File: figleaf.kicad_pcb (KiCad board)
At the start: 2 copper layers, 150 x 105 mm, 31 parts, among them U1 Nice_Nano_V2_GRAZ

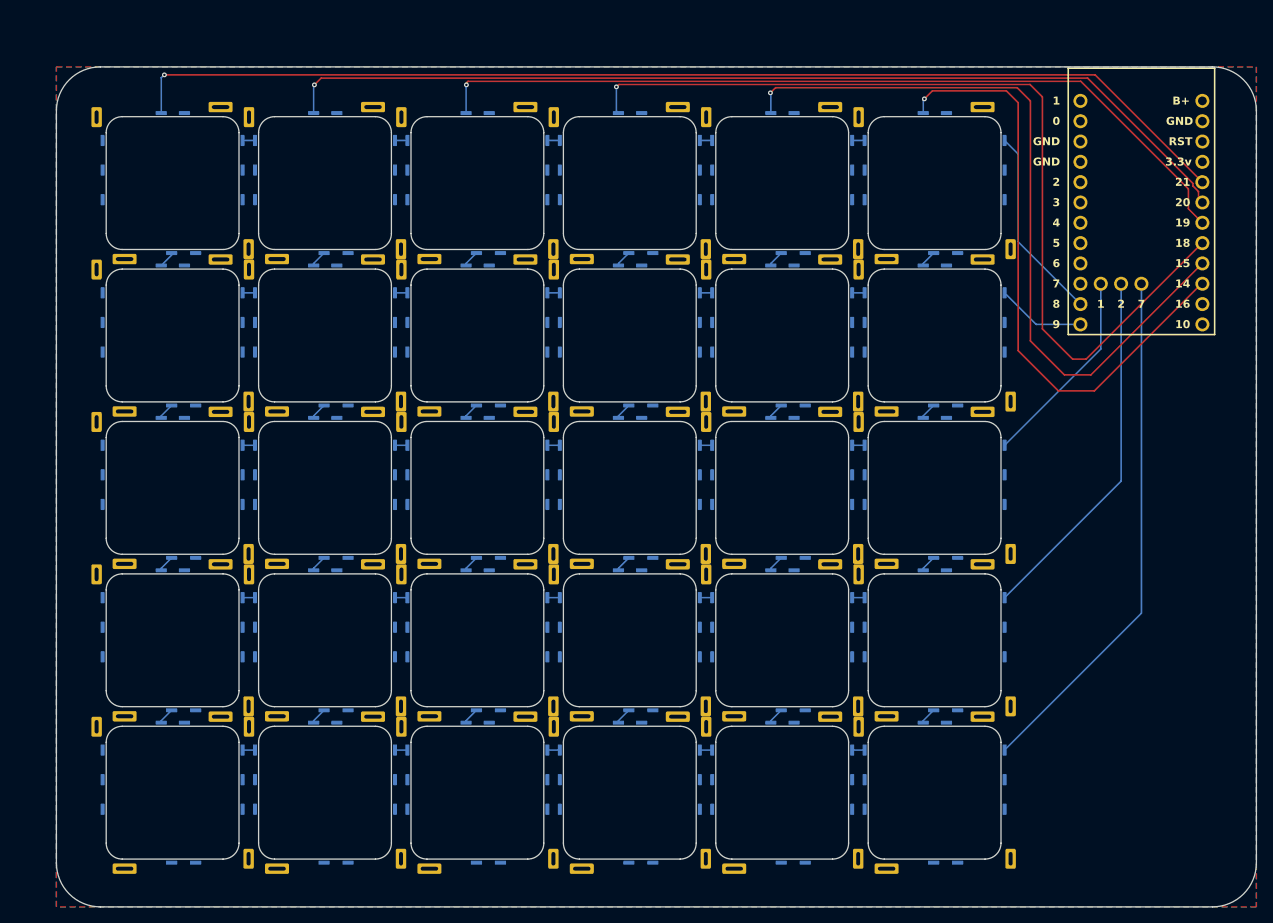
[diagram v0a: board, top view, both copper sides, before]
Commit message: PCB progress, switches to 19x19 pitch
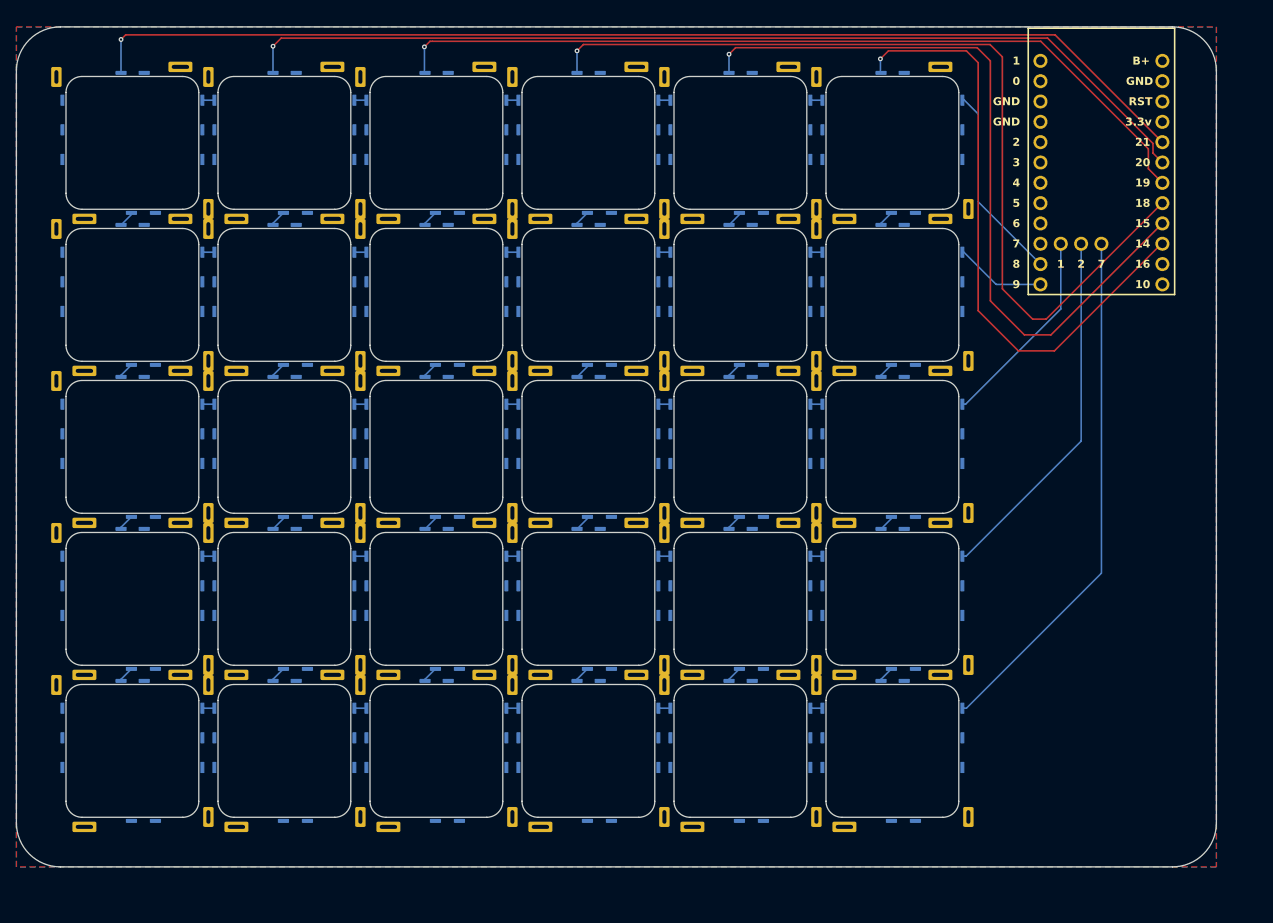
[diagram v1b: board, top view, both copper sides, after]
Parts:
- moved S30 7.42 mm to (129.5, 110.5)
- moved S24 7.39 mm to (129.5, 91.5)
- moved S29 7.39 mm to (110.5, 110.5)
- moved S18 7.35 mm to (129.5, 72.5)
- moved S23 7.35 mm to (110.5, 91.5)
- moved S28 7.35 mm to (91.5, 110.5)
- moved S12 7.32 mm to (129.5, 53.5)
- moved S17 7.32 mm to (110.5, 72.5)
- moved S27 7.32 mm to (72.5, 110.5)
- moved S22 7.32 mm to (91.5, 91.5)
- moved S6 7.29 mm to (129.5, 34.5)
- moved S11 7.28 mm to (110.5, 53.5)
- moved S26 7.28 mm to (53.5, 110.5)
- moved S16 7.28 mm to (91.5, 72.5)
- moved S21 7.28 mm to (72.5, 91.5)
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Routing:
- net col_3: track 114.0 -> 113.5 mm

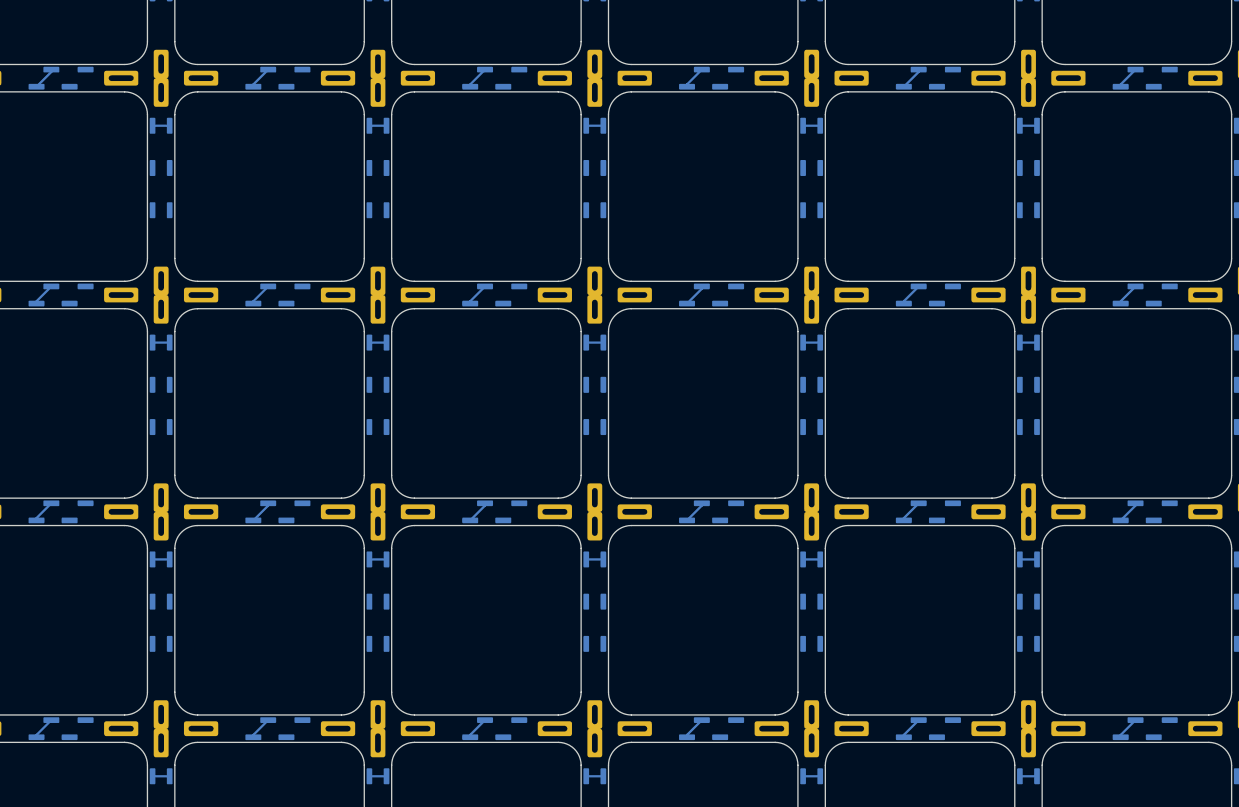
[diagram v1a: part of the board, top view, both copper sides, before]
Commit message: Add SW ground conn
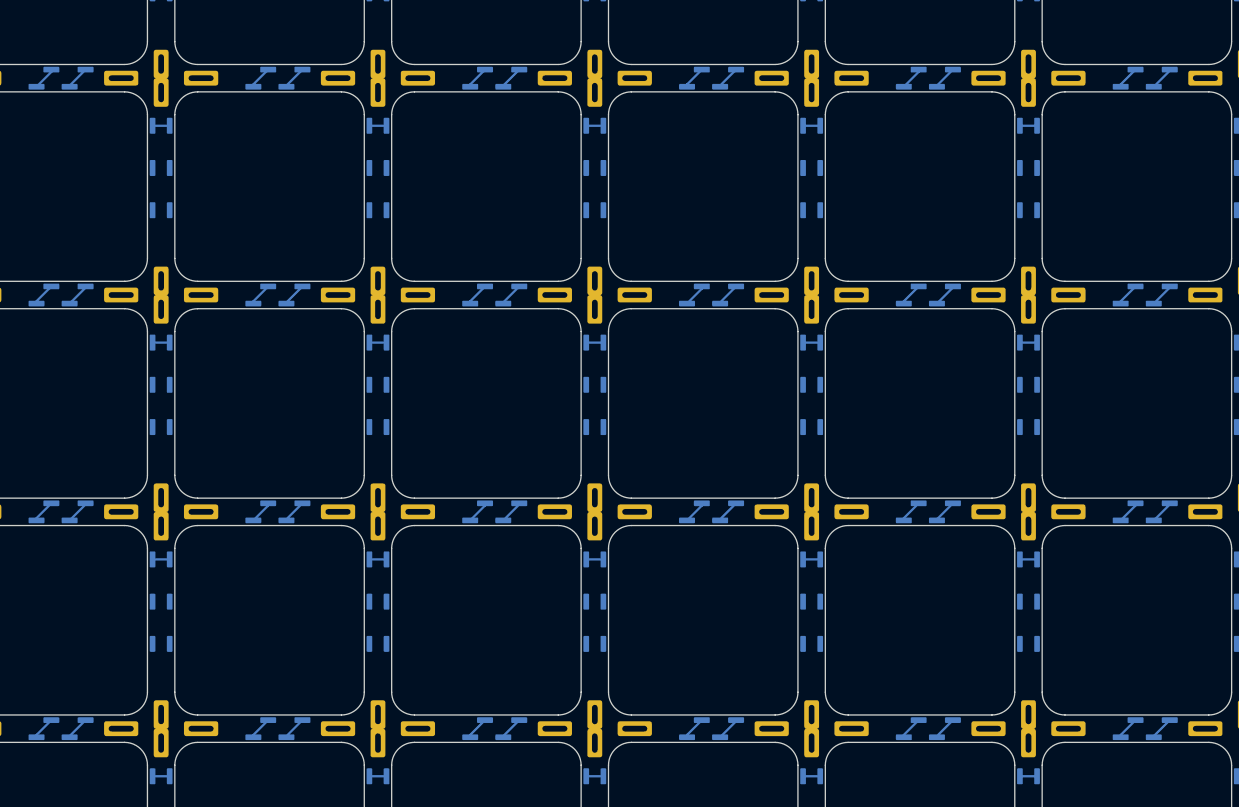
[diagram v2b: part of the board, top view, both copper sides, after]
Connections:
- S1 pad 5: unconnected-(S1-GND-Pad5) -> GND_L
- S1 pad 6: unconnected-(S1-GND-Pad6) -> Net-(S1-GND-Pad6)
- S10 pad 5: unconnected-(S10-GND-Pad5) -> Net-(S10-GND-Pad5)
- S10 pad 6: unconnected-(S10-GND-Pad6) -> Net-(S10-GND-Pad6)
- S11 pad 5: unconnected-(S11-GND-Pad5) -> Net-(S11-GND-Pad5)
- S11 pad 6: unconnected-(S11-GND-Pad6) -> Net-(S11-GND-Pad6)
- S12 pad 5: unconnected-(S12-GND-Pad5) -> Net-(S12-GND-Pad5)
- S12 pad 6: unconnected-(S12-GND-Pad6) -> Net-(S12-GND-Pad6)
- S13 pad 5: unconnected-(S13-GND-Pad5) -> Net-(S13-GND-Pad5)
- S13 pad 6: unconnected-(S13-GND-Pad6) -> Net-(S13-GND-Pad6)
- S14 pad 5: unconnected-(S14-GND-Pad5) -> Net-(S14-GND-Pad5)
- S14 pad 6: unconnected-(S14-GND-Pad6) -> Net-(S14-GND-Pad6)
- S15 pad 5: unconnected-(S15-GND-Pad5) -> Net-(S15-GND-Pad5)
- S15 pad 6: unconnected-(S15-GND-Pad6) -> Net-(S15-GND-Pad6)
- S16 pad 5: unconnected-(S16-GND-Pad5) -> Net-(S10-GND-Pad6)
- S16 pad 6: unconnected-(S16-GND-Pad6) -> Net-(S16-GND-Pad6)
- S17 pad 5: unconnected-(S17-GND-Pad5) -> Net-(S11-GND-Pad6)
- S17 pad 6: unconnected-(S17-GND-Pad6) -> Net-(S17-GND-Pad6)
- S18 pad 5: unconnected-(S18-GND-Pad5) -> Net-(S12-GND-Pad6)
- S18 pad 6: unconnected-(S18-GND-Pad6) -> Net-(S18-GND-Pad6)
- S19 pad 5: unconnected-(S19-GND-Pad5) -> Net-(S13-GND-Pad6)
- S19 pad 6: unconnected-(S19-GND-Pad6) -> Net-(S19-GND-Pad6)
- S2 pad 5: unconnected-(S2-GND-Pad5) -> GND_L
- S2 pad 6: unconnected-(S2-GND-Pad6) -> Net-(S2-GND-Pad6)
- S20 pad 5: unconnected-(S20-GND-Pad5) -> Net-(S14-GND-Pad6)
- S20 pad 6: unconnected-(S20-GND-Pad6) -> Net-(S20-GND-Pad6)
- S21 pad 5: unconnected-(S21-GND-Pad5) -> Net-(S15-GND-Pad6)
- S21 pad 6: unconnected-(S21-GND-Pad6) -> Net-(S21-GND-Pad6)
- S22 pad 5: unconnected-(S22-GND-Pad5) -> Net-(S16-GND-Pad6)
- S22 pad 6: unconnected-(S22-GND-Pad6) -> Net-(S22-GND-Pad6)
- S23 pad 5: unconnected-(S23-GND-Pad5) -> Net-(S17-GND-Pad6)
- S23 pad 6: unconnected-(S23-GND-Pad6) -> Net-(S23-GND-Pad6)
- S24 pad 5: unconnected-(S24-GND-Pad5) -> Net-(S18-GND-Pad6)
- S24 pad 6: unconnected-(S24-GND-Pad6) -> Net-(S24-GND-Pad6)
- S25 pad 5: unconnected-(S25-GND-Pad5) -> Net-(S19-GND-Pad6)
- S25 pad 6: unconnected-(S25-GND-Pad6) -> GND_L
- S26 pad 5: unconnected-(S26-GND-Pad5) -> Net-(S20-GND-Pad6)
- S26 pad 6: unconnected-(S26-GND-Pad6) -> GND_L
- S27 pad 5: unconnected-(S27-GND-Pad5) -> Net-(S21-GND-Pad6)
- S27 pad 6: unconnected-(S27-GND-Pad6) -> GND_L
- S28 pad 5: unconnected-(S28-GND-Pad5) -> Net-(S22-GND-Pad6)
- S28 pad 6: unconnected-(S28-GND-Pad6) -> GND_L
- S29 pad 5: unconnected-(S29-GND-Pad5) -> Net-(S23-GND-Pad6)
- S29 pad 6: unconnected-(S29-GND-Pad6) -> GND_L
- S3 pad 5: unconnected-(S3-GND-Pad5) -> GND_L
- S3 pad 6: unconnected-(S3-GND-Pad6) -> Net-(S3-GND-Pad6)
- S30 pad 5: unconnected-(S30-GND-Pad5) -> Net-(S24-GND-Pad6)
- S30 pad 6: unconnected-(S30-GND-Pad6) -> GND_L
- S4 pad 5: unconnected-(S4-GND-Pad5) -> GND_L
- S4 pad 6: unconnected-(S4-GND-Pad6) -> Net-(S10-GND-Pad5)
- S5 pad 5: unconnected-(S5-GND-Pad5) -> GND_L
- S5 pad 6: unconnected-(S5-GND-Pad6) -> Net-(S11-GND-Pad5)
- S6 pad 5: unconnected-(S6-GND-Pad5) -> GND_L
- S6 pad 6: unconnected-(S6-GND-Pad6) -> Net-(S12-GND-Pad5)
- S7 pad 5: unconnected-(S7-GND-Pad5) -> Net-(S1-GND-Pad6)
- S7 pad 6: unconnected-(S7-GND-Pad6) -> Net-(S13-GND-Pad5)
- S8 pad 5: unconnected-(S8-GND-Pad5) -> Net-(S2-GND-Pad6)
- S8 pad 6: unconnected-(S8-GND-Pad6) -> Net-(S14-GND-Pad5)
- S9 pad 5: unconnected-(S9-GND-Pad5) -> Net-(S3-GND-Pad6)
- S9 pad 6: unconnected-(S9-GND-Pad6) -> Net-(S15-GND-Pad5)
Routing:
- net Net-(S2-GND-Pad6): track 0.00 -> 2.08 mm
- net Net-(S14-GND-Pad5): track 0.00 -> 2.08 mm
- net Net-(S13-GND-Pad5): track 0.00 -> 2.08 mm
- net Net-(S12-GND-Pad6): track 0.00 -> 2.08 mm
- net Net-(S12-GND-Pad5): track 0.00 -> 2.08 mm
- net Net-(S1-GND-Pad6): track 0.00 -> 2.08 mm
- net Net-(S24-GND-Pad6): track 0.00 -> 2.08 mm
- net Net-(S20-GND-Pad6): track 0.00 -> 2.08 mm
- net Net-(S19-GND-Pad6): track 0.00 -> 2.08 mm
- net Net-(S18-GND-Pad6): track 0.00 -> 2.08 mm
- net Net-(S14-GND-Pad6): track 0.00 -> 2.08 mm
- net Net-(S13-GND-Pad6): track 0.00 -> 2.08 mm
- net Net-(S3-GND-Pad6): track 0.00 -> 2.08 mm
- net Net-(S15-GND-Pad5): track 0.00 -> 2.08 mm
- net Net-(S11-GND-Pad6): track 0.00 -> 2.08 mm
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
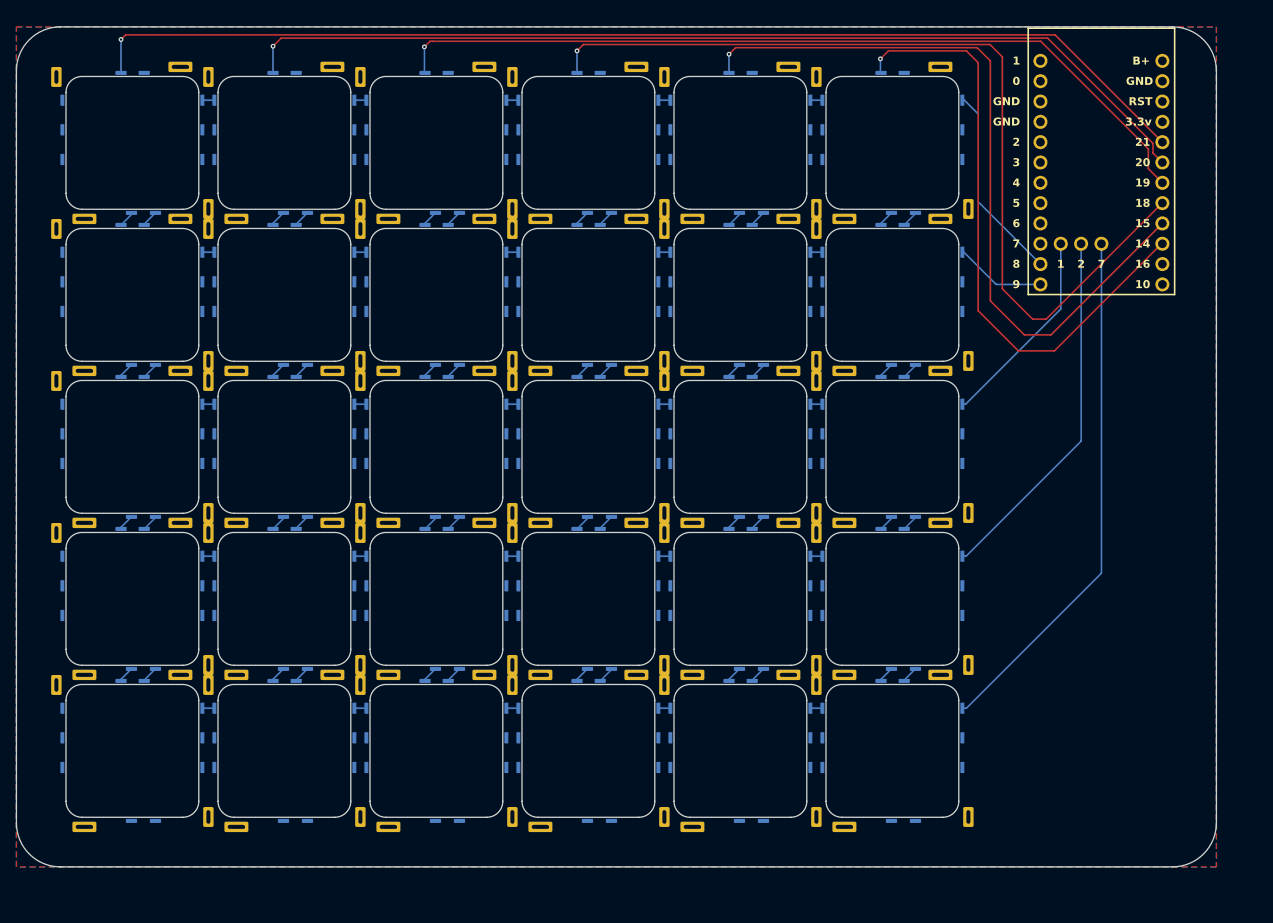
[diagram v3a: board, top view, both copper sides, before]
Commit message: swap to my OKM footprint + updated TH pads for switch lugs
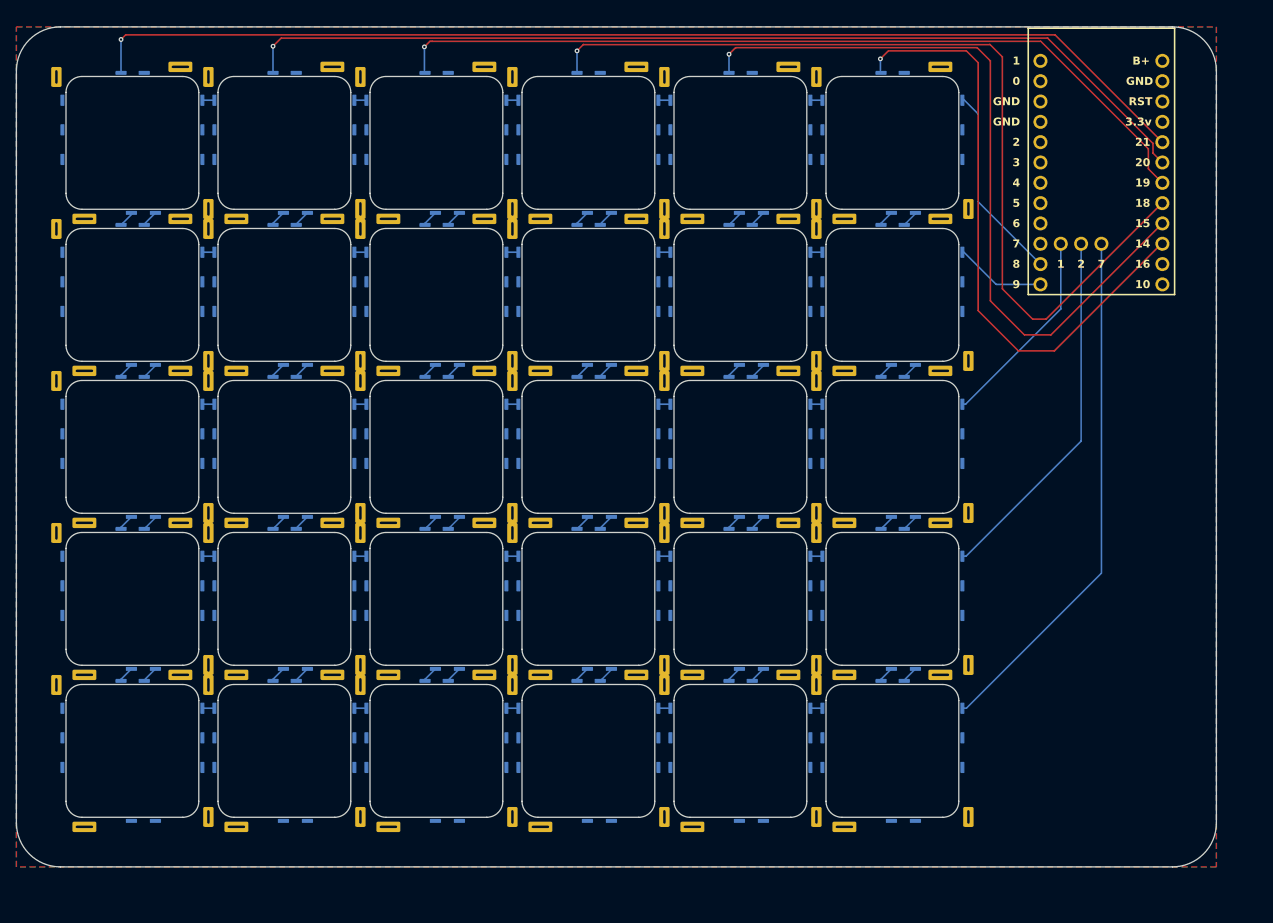
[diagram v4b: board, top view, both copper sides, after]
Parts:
- S1, S10, S11, S12, S13, S14, S15, S16, S17, S18, S19, S2, S20, S21, S22, S23, S24, S25, S26, S27, S28, S29, S3, S30, S4, S5, S6, S7, S8, S9: footprint Graz_Footprints:One Key Module -> Graz_Footprints:One Key Module Graz

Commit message: fix all DRC issues
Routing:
- net GND_L: track 0.00 -> 29.6 mm
- net col_0: track 140.1 -> 142.2 mm, vias 1 -> 2
- net col_1: track 122.1 -> 123.8 mm, vias 1 -> 2
- net col_2: track 104.6 -> 105.9 mm, vias 1 -> 2
- net col_5: track 76.7 -> 75.6 mm
- net col_4: track 95.1 -> 94.1 mm
- net col_3: track 113.5 -> 112.7 mm
